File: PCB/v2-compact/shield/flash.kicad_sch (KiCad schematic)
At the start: 0 parts

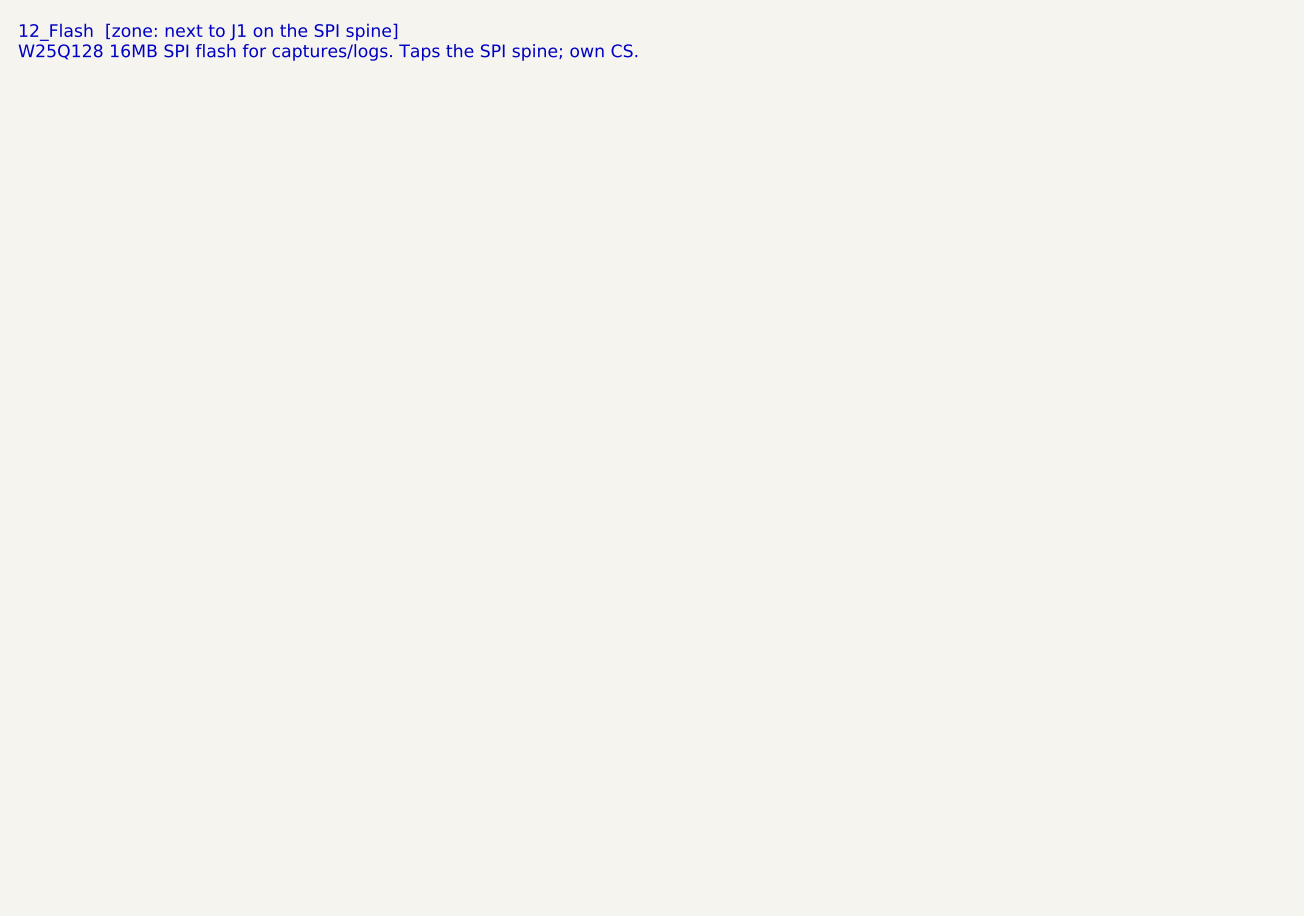
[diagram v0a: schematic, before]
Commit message: Schematics: fix hierarchy load, add verified generator, capture flash sheet
The v2 schematic roots were missing the per-sheet (instances) block, so the
projects would not load in KiCad (kicad-cli failed on both). Regenerate both
roots in a verified format (netlist export now succeeds on both boards).

Populate the first sub-sheet (12_Flash) as the proven pattern: real W25Q128
symbol, decoupling, wired to the SPI spine and power by global labels. Verified
by netlist (U12 pins map to FLASH_CS / SPI_SCK / SPI_MOSI / SPI_MISO / +3V3 / GND).
Remaining sub-sheets to follow the same pattern.
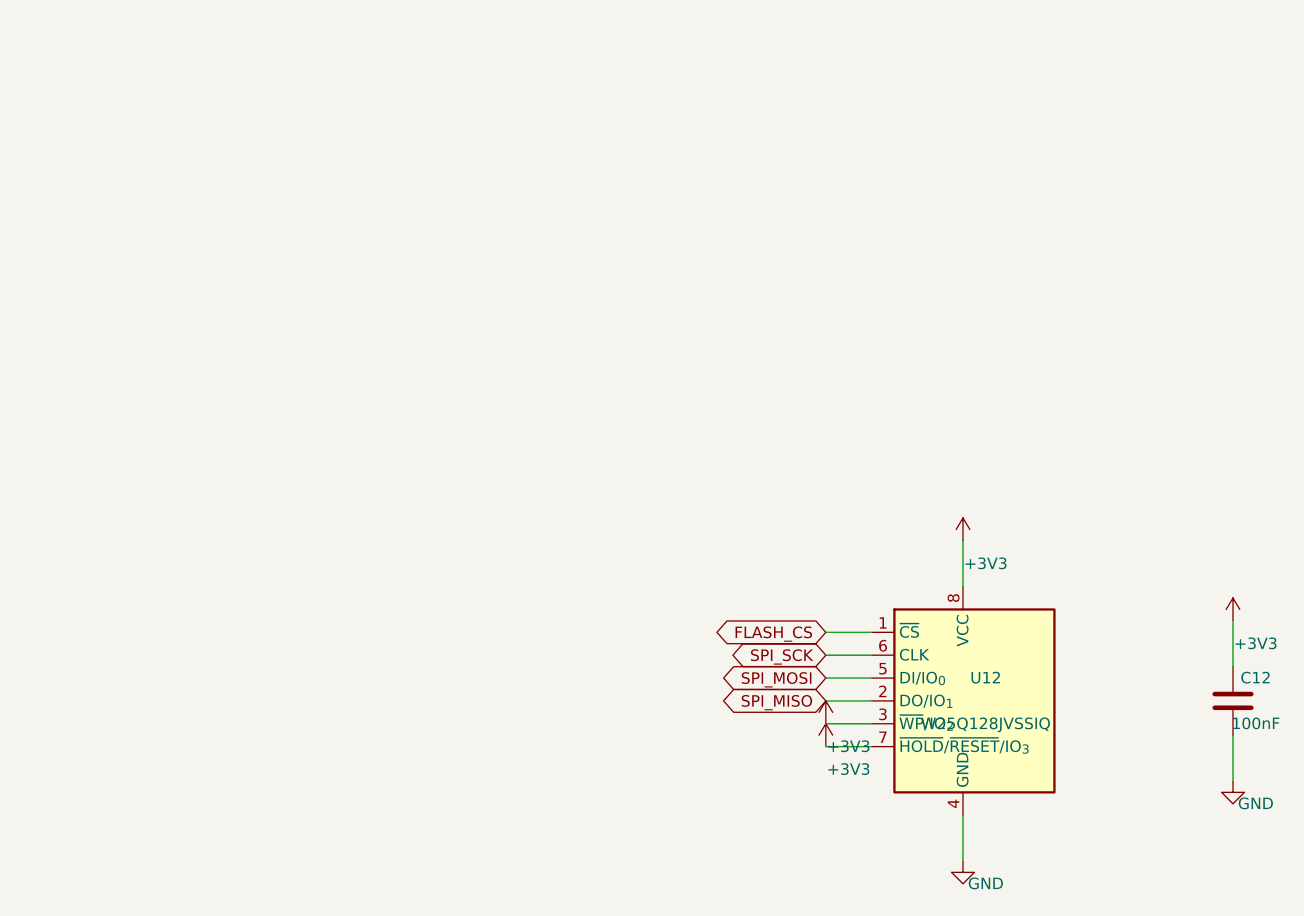
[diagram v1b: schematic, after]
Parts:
- added C12: 100nF, Capacitor_SMD:C_0402_1005Metric, symbol Device:C
- added U12: W25Q128JVSSIQ, Package_SO:SOIC-8_3.9x4.9mm_P1.27mm, symbol Memory_Flash:W25Q128JVS
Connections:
- new net +3V3: C12.1, U12.3 (~{WP}/IO_{2}), U12.7 (~{HOLD}/~{RESET}/IO_{3}), U12.8 (VCC)
- new net FLASH_CS: U12.1 (~{CS})
- new net GND: C12.2, U12.4 (GND)
- new net SPI_MISO: U12.2 (DO/IO_{1})
- new net SPI_MOSI: U12.5 (DI/IO_{0})
- new net SPI_SCK: U12.6 (CLK)
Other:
- note removed: "12_Flash [zone: next to J1 on the SPI spine] W25Q128 16MB SPI flash for captures/logs. Taps the SPI spine; own CS."
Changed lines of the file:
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@@
   (paper "A4")
   (title_block (title "12_Flash_Storage") (company "YurilLAB"))
-  (text "12_Flash  [zone: next to J1 on the SPI spine]
-W25Q128 16MB SPI flash for captures/logs. Taps the SPI spine; own CS." (at 15 15 0)
-    (effects (font (size 1.4 1.4)) (justify left top)))
+  (symbol (lib_id "Memory_Flash:W25Q128JVS") (at 120 90 0) (unit 1)
+    (in_bom yes) (on_board yes) (dnp no)
+    (property "Reference" "U12" (at 122.54 87.46 0) (effects (font (size 1.27 1.27))))
+    (property "Value" "W25Q128JVSSIQ" (at 122.54 92.54 0) (effects (font (size 1.27 1.27))))
+    (property "Footprint" "Package_SO:SOIC-8_3.9x4.9mm_P1.27mm" (at 120 90 0) (effects (font (size 1.27 1.27)) hide))
+    (pin "1")
+    (pin "2")
+    (pin "3")
+    (pin "4")
+    (pin "5")
+    (pin "6")
+    (pin "7")
+    (pin "8")
+    (instances (project "SnowOwl-Shield" (path "/4e94e7f7-7328-40c5-88b8-5d45dab38b09" (reference "U12") (unit 1))))
+  )
+  (wire (pts (xy 109.84 82.38) (xy 104.76 82.38)) (stroke (width 0) (type default)))
+  (global_label "FLASH_CS" (shape bidirectional) (at 104.76 82.38 180) (fields_autoplaced)
+    (effects (font (size 1.27 1.27)) (justify right)))
+  (wire (pts (xy 109.84 90) (xy 104.76 90)) (stroke (width 0) (type default)))
+  (global_label "SPI_MISO" (shape bidirectional) (at 104.76 90 180) (fields_autoplaced)
+    (effects (font (size 1.27 1.27)) (justify right)))
+  (wire (pts (xy 109.84 92.54) (xy 104.76 92.54)) (stroke (width 0) (type default)))
+  (symbol (lib_id "power:+3V3") (at 104.76 92.54 0) (unit 1)
+    (in_bom yes) (on_board yes) (dnp no)
+    (property "Reference" "#PWR001" (at 107.3 90 0) (effects (font (size 1.27 1.27)) hide))
+    (property "Value" "+3V3" (at 107.3 95.08 0) (effects (font (size 1.27 1.27))))
+    (property "Footprint" "" (at 104.76 92.54 0) (effects (font (size 1.27 1.27)) hide))
+    (pin "1")
+    (instances (project "SnowOwl-Shield" (path "/4e94e7f7-7328-40c5-88b8-5d45dab38b09" (reference "#PWR001") (unit 1))))
+  )
+  (wire (pts (xy 120 102.7) (xy 120 107.78)) (stroke (width 0) (type default)))
+  (symbol (lib_id "power:GND") (at 120 107.78 0) (unit 1)
+    (in_bom yes) (on_board yes) (dnp no)
+    (property "Reference" "#PWR002" (at 122.54 105.24 0) (effects (font (size 1.27 1.27)) hide))
+    (property "Value" "GND" (at 122.54 110.32 0) (effects (font (size 1.27 1.27))))
+    (property "Footprint" "" (at 120 107.78 0) (effects (font (size 1.27 1.27)) hide))
+    (pin "1")
+    (instances (project "SnowOwl-Shield" (path "/4e94e7f7-7328-40c5-88b8-5d45dab38b09" (reference "#PWR002") (unit 1))))
+  )
+  (wire (pts (xy 109.84 87.46) (xy 104.76 87.46)) (stroke (width 0) (type default)))
+  (global_label "SPI_MOSI" (shape bidirectional) (at 104.76 87.46 180) (fields_autoplaced)
+    (effects (font (size 1.27 1.27)) (justify right)))
+  (wire (pts (xy 109.84 84.92) (xy 104.76 84.92)) (stroke (width 0) (type default)))
+  (global_label "SPI_SCK" (shape bidirectional) (at 104.76 84.92 180) (fields_autoplaced)
+    (effects (font (size 1.27 1.27)) (justify right)))
+  (wire (pts (xy 109.84 95.08) (xy 104.76 95.08)) (stroke (width 0) (type default)))
+  (symbol (lib_id "power:+3V3") (at 104.76 95.08 0) (unit 1)
+    (in_bom yes) (on_board yes) (dnp no)
+    (property "Reference" "#PWR003" (at 107.3 92.54 0) (effects (font (size 1.27 1.27)) hide))
+    (property "Value" "+3V3" (at 107.3 97.62 0) (effects (font (size 1.27 1.27))))
+    (property "Footprint" "" (at 104.76 95.08 0) (effects (font (size 1.27 1.27)) hide))
+    (pin "1")
+    (instances (project "SnowOwl-Shield" (path "/4e94e7f7-7328-40c5-88b8-5d45dab38b09" (reference "#PWR003") (unit 1))))
+  )
+  (wire (pts (xy 120 77.3) (xy 120 72.22)) (stroke (width 0) (type default)))
+  (symbol (lib_id "power:+3V3") (at 120 72.22 0) (unit 1)
+    (in_bom yes) (on_board yes) (dnp no)
+    (property "Reference" "#PWR004" (at 122.54 69.68 0) (effects (font (size 1.27 1.27)) hide))
+    (property "Value" "+3V3" (at 122.54 74.76 0) (effects (font (size 1.27 1.27))))
+    (property "Footprint" "" (at 120 72.22 0) (effects (font (size 1.27 1.27)) hide))
+    (pin "1")
+    (instances (project "SnowOwl-Shield" (path "/4e94e7f7-7328-40c5-88b8-5d45dab38b09" (reference "#PWR004") (unit 1))))
+  )
+  (symbol (lib_id "Device:C") (at 150 90 0) (unit 1)
+    (in_bom yes) (on_board yes) (dnp no)
+    (property "Reference" "C12" (at 152.54 87.46 0) (effects (font (size 1.27 1.27))))
+    (property "Value" "100nF" (at 152.54 92.54 0) (effects (font (size 1.27 1.27))))
+    (property "Footprint" "Capacitor_SMD:C_0402_1005Metric" (at 150 90 0) (effects (font (size 1.27 1.27)) hide))
+    (pin "1")
+    (pin "2")
+    (instances (project "SnowOwl-Shield" (path "/4e94e7f7-7328-40c5-88b8-5d45dab38b09" (reference "C12") (unit 1))))
+  )
+  (wire (pts (xy 150 86.19) (xy 150 81.11)) (stroke (width 0) (type default)))
+  (symbol (lib_id "power:+3V3") (at 150 81.11 0) (unit 1)
+    (in_bom yes) (on_board yes) (dnp no)
+    (property "Reference" "#PWR005" (at 152.54 78.57 0) (effects (font (size 1.27 1.27)) hide))
+    (property "Value" "+3V3" (at 152.54 83.65 0) (effects (font (size 1.27 1.27))))
+    (property "Footprint" "" (at 150 81.11 0) (effects (font (size 1.27 1.27)) hide))
+    (pin "1")
+    (instances (project "SnowOwl-Shield" (path "/4e94e7f7-7328-40c5-88b8-5d45dab38b09" (reference "#PWR005") (unit 1))))
+  )
+  (wire (pts (xy 150 93.81) (xy 150 98.89)) (stroke (width 0) (type default)))
+  (symbol (lib_id "power:GND") (at 150 98.89 0) (unit 1)
+    (in_bom yes) (on_board yes) (dnp no)
+    (property "Reference" "#PWR006" (at 152.54 96.35 0) (effects (font (size 1.27 1.27)) hide))
+    (property "Value" "GND" (at 152.54 101.43 0) (effects (font (size 1.27 1.27))))
+    (property "Footprint" "" (at 150 98.89 0) (effects (font (size 1.27 1.27)) hide))
+    (pin "1")
+    (instances (project "SnowOwl-Shield" (path "/4e94e7f7-7328-40c5-88b8-5d45dab38b09" (reference "#PWR006") (unit 1))))
+  )
   (sheet_instances (path "/" (page "1")))
 )

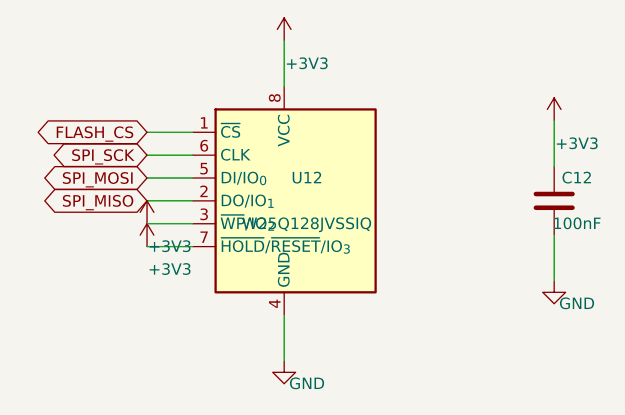
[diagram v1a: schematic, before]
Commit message: Schematics: custom symbols + footprint lib + backbone/nRF24/iButton sheets
- Add SnowOwl.kicad_sym (nRF24 + CC1101 module symbols; MISO tri-state for the
  shared SPI bus) and SnowOwl.pretty with the 2x10 stack-header footprint,
  registered via project sym-lib-table / fp-lib-table on both boards.
- Capture sheets, each netlist- and ERC-checked:
  - J1 stack header (both boards) wired to the locked pinout (the interconnect
    backbone: power + I2C + S3<->C5 UART + S3<->RV1106 UART + IR + 1-Wire)
  - nRF24 x3 on the shared SPI spine (per-radio CE/CSN/IRQ) with decoupling
  - iButton 1-Wire with pull-up
- Engine: snap all placements to the 1.27mm grid (clears 103 off-grid warnings);
  globally-unique power-symbol refs.

Remaining ERC items are expected for a partial design (isolated labels resolve
when both ends of a net are captured; power-not-driven clears with the power sheet).
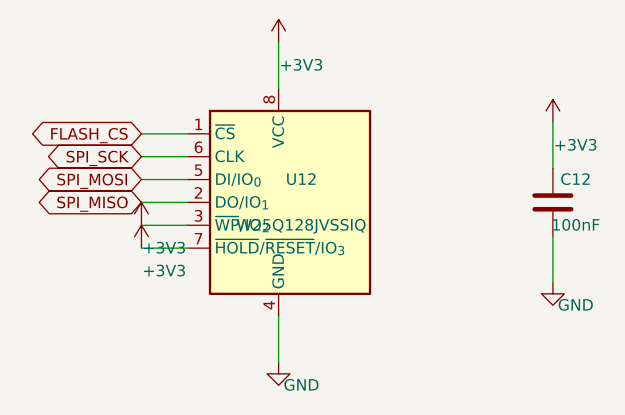
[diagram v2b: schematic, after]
